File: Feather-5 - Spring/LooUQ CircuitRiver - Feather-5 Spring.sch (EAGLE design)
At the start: 11 parts, among them J1 FEATHERHOST-S, J2 FEATHERHOST-L, J3 CR-SPRING_HEADER, J4 JST_PH-2_T/H, J5 JST_PH-2_T/H, J6 QWIIC_VERTICAL, J7 CR-RAPIDSIO_VERTICAL, J8 DNF, P3 SLEEP

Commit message: Updated Feathers
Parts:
- added P1: DNF, common:~RESET
- added P2: DNF, common:GND
- P3: value SLEEP -> DNF
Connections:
- new net Net_0: J2.!RESET, P1.1
- new net Net_24: J2.AREF, J8.P1
- net Net_3v3: now also J8.P2; no longer J8.P1
- net Net_GND: now also P2.1; no longer J8.P2
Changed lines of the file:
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@@
 <part name="LG1" library="common" deviceset="LOOUQ_LOGO" device=""/>
 <part name="LG2" library="common" deviceset="CIRCUITRIVER_LOGO" device=""/>
-<part name="P3" library="common" deviceset="SLEEP" device=""/>
+<part name="P1" library="common" deviceset="~RESET" device="" value="DNF"/>
+<part name="P2" library="common" deviceset="GND" device="" value="DNF"/>
+<part name="P3" library="common" deviceset="SLEEP" device="" value="DNF"/>
 </parts>
 <modules/>
@@
 <instance part="LG1" gate="PART_1" x="91.122" y="86.995"/>
 <instance part="LG2" gate="PART_1" x="91.587" y="80.96"/>
-<instance part="P3" gate="BRKOUTPAD" x="101.362" y="-6.033" rot="R270"/>
+<instance part="P1" gate="BRKOUTPAD" x="-57.229" y="-12.7" rot="R90"/>
+<instance part="P2" gate="BRKOUTPAD" x="-57.229" y="-85.566" rot="R90"/>
+<instance part="P3" gate="BRKOUTPAD" x="101.362" y="-5.874" rot="R270"/>
 </instances>
 <busses/>
@@
 <net name="Net_22" class="0">
 <segment>
-<wire layer="91" width="0.25" x1="106.204" y1="-5.95" x2="104.934" y2="-6.033"/>
+<wire layer="91" width="0.25" x1="106.204" y1="-5.95" x2="104.934" y2="-5.874"/>
 <wire layer="91" width="0.25" x1="106.204" y1="-5.95" x2="106.986" y2="-5.95"/>
 <pinref part="P3" gate="BRKOUTPAD" pin="1"/>
@@
 <net name="Net_3v3" class="1">
 <segment>
-<wire layer="91" width="0.25" x1="-77.153" y1="-19.844" x2="-82.709" y2="-19.844"/>
-<wire layer="91" width="0.25" x1="-82.709" y1="-19.844" x2="-82.709" y2="-17.308"/>
-<wire layer="91" width="0.25" x1="-82.709" y1="-17.308" x2="-85.563" y2="-17.308"/>
-<pinref part="J8" gate="PART_1" pin="P1"/>
-<pinref part="J2" gate="PART_1" pin="+3V3"/>
 <wire layer="91" width="0.25" x1="-100.965" y1="-5.239" x2="-82.709" y2="-5.239"/>
 <wire layer="91" width="0.25" x1="-82.709" y1="-5.239" x2="-82.709" y2="-17.308"/>
+<wire layer="91" width="0.25" x1="-82.709" y1="-17.308" x2="-82.709" y2="-17.304"/>
+<wire layer="91" width="0.25" x1="-82.709" y1="-17.304" x2="-82.709" y2="-82.605"/>
+<wire layer="91" width="0.25" x1="-82.709" y1="-82.605" x2="-104.989" y2="-82.605"/>
 <pinref part="J6" gate="PART_1" pin="3v3"/>
+<pinref part="J7" gate="PART_1" pin="3v3"/>
+<wire layer="91" width="0.25" x1="-77.153" y1="-17.304" x2="-82.709" y2="-17.304"/>
+<pinref part="J8" gate="PART_1" pin="P2"/>
+<junction x="-82.709" y="-17.304"/>
+<wire layer="91" width="0.25" x1="-85.563" y1="-17.308" x2="-82.709" y2="-17.308"/>
+<pinref part="J2" gate="PART_1" pin="+3V3"/>
 <junction x="-82.709" y="-17.308"/>
-<wire layer="91" width="0.25" x1="-82.709" y1="-19.844" x2="-82.709" y2="-82.605"/>
-<wire layer="91" width="0.25" x1="-82.709" y1="-82.605" x2="-104.989" y2="-82.605"/>
-<pinref part="J7" gate="PART_1" pin="3v3"/>
-<junction x="-82.709" y="-19.844"/>
 </segment>
 </net>
 <net name="Net_GND" class="1">
 <segment>
-<wire layer="91" width="0.25" x1="-85.542" y1="-22.388" x2="-81.28" y2="-22.388"/>
-<wire layer="91" width="0.25" x1="-81.28" y1="-22.388" x2="-52.229" y2="-22.388"/>
+<wire layer="91" width="0.25" x1="-85.542" y1="-22.388" x2="-80.962" y2="-22.388"/>
+<wire layer="91" width="0.25" x1="-80.962" y1="-22.388" x2="-52.229" y2="-22.388"/>
 <wire layer="91" width="0.25" x1="-52.229" y1="-22.388" x2="-52.229" y2="-9.684"/>
 <wire layer="91" width="0.25" x1="-52.229" y1="-9.684" x2="-52.229" y2="44.05"/>
@@
 <pinref part="J5" gate="PART_1" pin="P2"/>
 <junction x="-52.229" y="44.05"/>
-<wire layer="91" width="0.25" x1="-100.965" y1="-9.684" x2="-80.327" y2="-9.684"/>
-<wire layer="91" width="0.25" x1="-80.327" y1="-9.684" x2="-52.229" y2="-9.684"/>
+<wire layer="91" width="0.25" x1="-100.965" y1="-9.684" x2="-52.229" y2="-9.684"/>
 <pinref part="J6" gate="PART_1" pin="GND"/>
 <junction x="-52.229" y="-9.684"/>
-<wire layer="91" width="0.25" x1="-77.153" y1="-17.304" x2="-80.327" y2="-17.304"/>
-<wire layer="91" width="0.25" x1="-80.327" y1="-17.304" x2="-80.327" y2="-9.684"/>
-<pinref part="J8" gate="PART_1" pin="P2"/>
-<junction x="-80.327" y="-9.684"/>
-<wire layer="91" width="0.25" x1="-81.28" y1="-22.388" x2="-81.28" y2="-85.551"/>
-<wire layer="91" width="0.25" x1="-81.28" y1="-85.551" x2="-104.989" y2="-85.551"/>
+<wire layer="91" width="0.25" x1="-80.962" y1="-22.388" x2="-80.962" y2="-85.551"/>
+<wire layer="91" width="0.25" x1="-80.962" y1="-85.551" x2="-104.989" y2="-85.551"/>
 <pinref part="J7" gate="PART_1" pin="GND"/>
-<junction x="-81.28" y="-22.388"/>
+<junction x="-80.962" y="-22.388"/>
+<wire layer="91" width="0.25" x1="-62.071" y1="-85.551" x2="-60.801" y2="-85.566"/>
+<wire layer="91" width="0.25" x1="-62.071" y1="-85.551" x2="-80.962" y2="-85.551"/>
+<pinref part="P2" gate="BRKOUTPAD" pin="1"/>
+<junction x="-80.962" y="-85.551"/>
 </segment>
 </net>
@@
 </segment>
 </net>
+<net name="Net_24" class="0">
+<segment>
+<wire layer="91" width="0.25" x1="-78.423" y1="-19.848" x2="-77.153" y2="-19.844"/>
+<wire layer="91" width="0.25" x1="-78.423" y1="-19.848" x2="-85.552" y2="-19.848"/>
+<pinref part="J8" gate="PART_1" pin="P1"/>
+<pinref part="J2" gate="PART_1" pin="AREF"/>
+</segment>
+</net>
+<net name="Net_0" class="0">
+<segment>
+<wire layer="91" width="0.25" x1="-60.801" y1="-12.7" x2="-80.804" y2="-12.7"/>
+<wire layer="91" width="0.25" x1="-80.804" y1="-12.7" x2="-80.804" y2="-14.768"/>
+<wire layer="91" width="0.25" x1="-80.804" y1="-14.768" x2="-85.573" y2="-14.768"/>
+<pinref part="P1" gate="BRKOUTPAD" pin="1"/>
+<pinref part="J2" gate="PART_1" pin="!RESET"/>
+</segment>
+</net>

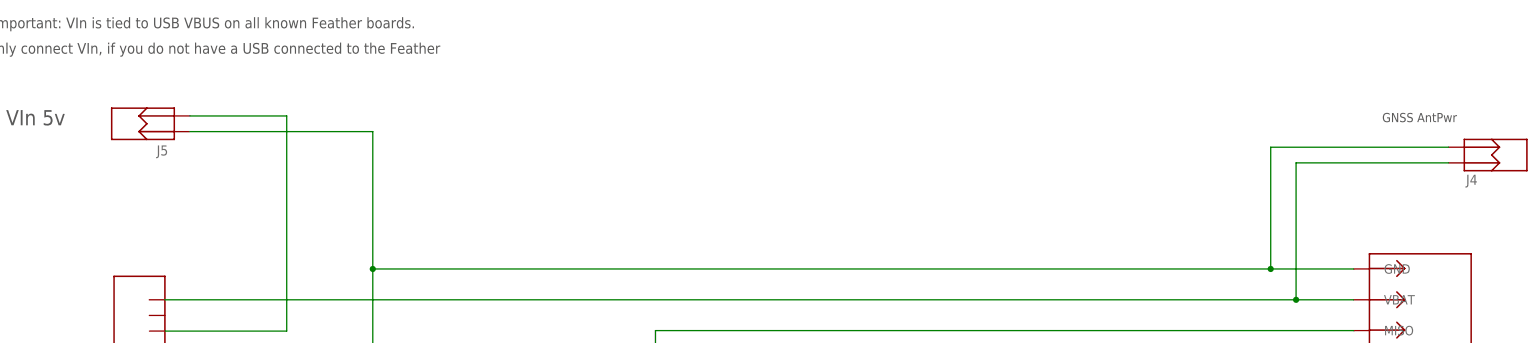
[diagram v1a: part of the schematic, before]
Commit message: Moved RapidsIO, chg L1 on F-630
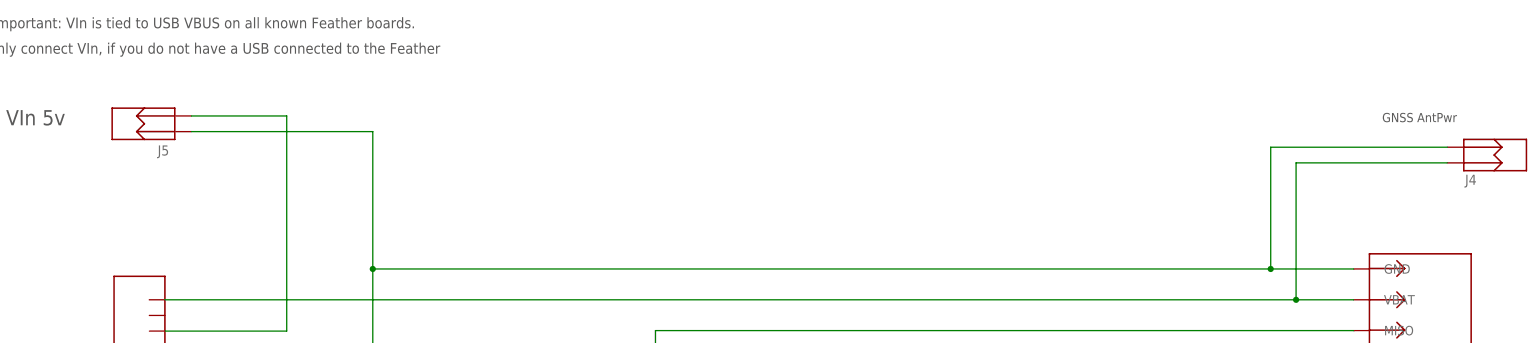
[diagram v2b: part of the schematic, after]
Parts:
- J4: value JST_PH-2_T/H -> JST_PH-2_R/A_T/H; device common:JST_PH-2_T/H -> common:JST_PH-2_R/A_T/H
- J5: value JST_PH-2_T/H -> JST_PH-2_VERT_T/H; device common:JST_PH-2_T/H -> common:JST_PH-2_VERT_T/H
- LG1: value LOOUQ_LOGO -> DNF
- LG2: value CIRCUITRIVER_LOGO -> DNF
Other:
- moved on the sheet: J4, J5
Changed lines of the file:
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@@
 <part name="J2" library="common" deviceset="FEATHERHOST-L" device=""/>
 <part name="J3" library="common" deviceset="CR-SPRING_HEADER" device=""/>
-<part name="J4" library="common" deviceset="JST_PH-2_T/H" device=""/>
-<part name="J5" library="common" deviceset="JST_PH-2_T/H" device=""/>
+<part name="J4" library="common" deviceset="JST_PH-2_R/A_T/H" device=""/>
+<part name="J5" library="common" deviceset="JST_PH-2_VERT_T/H" device=""/>
 <part name="J6" library="common" deviceset="QWIIC_VERTICAL" device=""/>
 <part name="J7" library="common" deviceset="CR-RAPIDSIO_VERTICAL" device=""/>
 <part name="J8" library="common" deviceset="2PIN_T/H_HEADER" device="" value="DNF"/>
-<part name="LG1" library="common" deviceset="LOOUQ_LOGO" device=""/>
-<part name="LG2" library="common" deviceset="CIRCUITRIVER_LOGO" device=""/>
+<part name="LG1" library="common" deviceset="LOOUQ_LOGO" device="" value="DNF"/>
+<part name="LG2" library="common" deviceset="CIRCUITRIVER_LOGO" device="" value="DNF"/>
 <part name="P1" library="common" deviceset="~RESET" device="" value="DNF"/>
 <part name="P2" library="common" deviceset="GND" device="" value="DNF"/>
@@
 <attribute name="NAME" value="J3" layer="95" x="109.448" y="-33.368" size="1.628" align="top-left"/>
 </instance>
-<instance part="J4" gate="PART_1" x="130.004" y="62.541" rot="R180">
-<attribute name="NAME" value="J4" layer="95" x="125.206" y="59.34" size="1.628" align="top-left"/>
-</instance>
-<instance part="J5" gate="PART_1" x="-89.528" y="67.615">
-<attribute name="NAME" value="J5" layer="95" x="-87.305" y="64.097" size="1.628" align="top-left"/>
+<instance part="J4" gate="PART_1" x="129.845" y="62.541">
+<attribute name="NAME" value="J4" layer="95" x="125.047" y="59.34" size="1.628" align="top-left"/>
+</instance>
+<instance part="J5" gate="PART_1" x="-89.369" y="67.615" rot="R180">
+<attribute name="NAME" value="J5" layer="95" x="-87.146" y="64.097" size="1.628" align="top-left"/>
 </instance>
 <instance part="J6" gate="PART_1" x="-107.56" y="-3.016" rot="R90">
@@
 <net name="Net_VBUS" class="1">
 <segment>
-<wire layer="91" width="0.25" x1="-81.908" y1="68.885" x2="-66.199" y2="68.885"/>
+<wire layer="91" width="0.25" x1="-81.67" y1="68.885" x2="-66.199" y2="68.885"/>
 <wire layer="91" width="0.25" x1="-66.199" y1="68.885" x2="-66.199" y2="33.969"/>
 <wire layer="91" width="0.25" x1="-66.199" y1="33.969" x2="-85.94" y2="33.969"/>
@@
 <pinref part="J2" gate="PART_1" pin="GND@2"/>
 <pinref part="J3" gate="PART_1" pin="GND"/>
-<wire layer="91" width="0.25" x1="122.384" y1="63.811" x2="93.504" y2="63.811"/>
+<wire layer="91" width="0.25" x1="122.145" y1="63.811" x2="93.504" y2="63.811"/>
 <wire layer="91" width="0.25" x1="93.504" y1="63.811" x2="93.504" y2="44.05"/>
 <pinref part="J4" gate="PART_1" pin="P2"/>
 <junction x="93.504" y="44.05"/>
-<wire layer="91" width="0.25" x1="-81.908" y1="66.345" x2="-52.229" y2="66.345"/>
+<wire layer="91" width="0.25" x1="-81.67" y1="66.345" x2="-52.229" y2="66.345"/>
 <wire layer="91" width="0.25" x1="-52.229" y1="66.345" x2="-52.229" y2="44.05"/>
 <pinref part="J5" gate="PART_1" pin="P2"/>
@@
 <pinref part="J1" gate="PART_1" pin="VBAT"/>
 <pinref part="J3" gate="PART_1" pin="VBAT"/>
-<wire layer="91" width="0.25" x1="122.384" y1="61.271" x2="97.621" y2="61.271"/>
+<wire layer="91" width="0.25" x1="122.145" y1="61.271" x2="97.621" y2="61.271"/>
 <wire layer="91" width="0.25" x1="97.621" y1="61.271" x2="97.621" y2="39.048"/>
 <pinref part="J4" gate="PART_1" pin="P1"/>
